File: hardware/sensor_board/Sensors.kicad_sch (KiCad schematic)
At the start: 12 parts

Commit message: all bricked...
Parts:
- gave numbers to parts that had none: 12

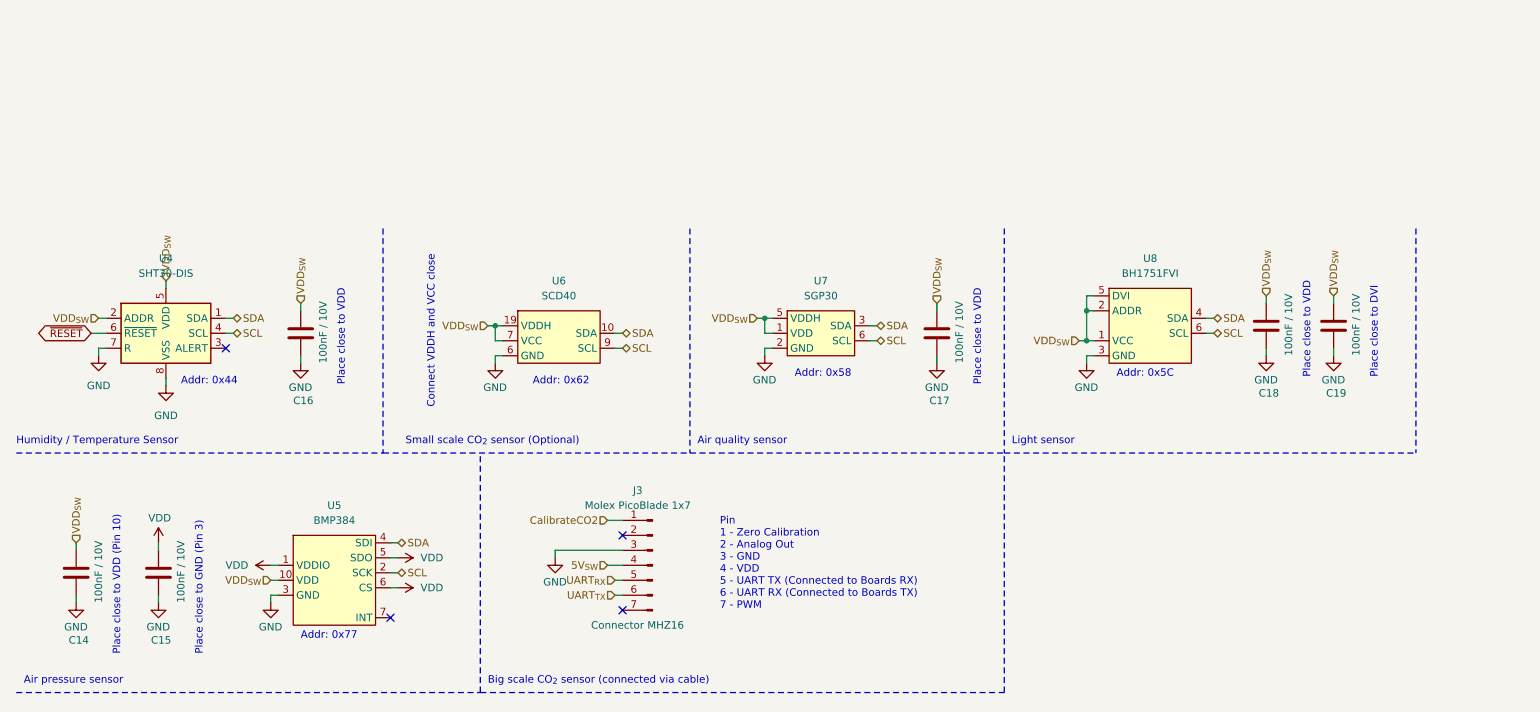
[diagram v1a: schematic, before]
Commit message: solved issues with ERC
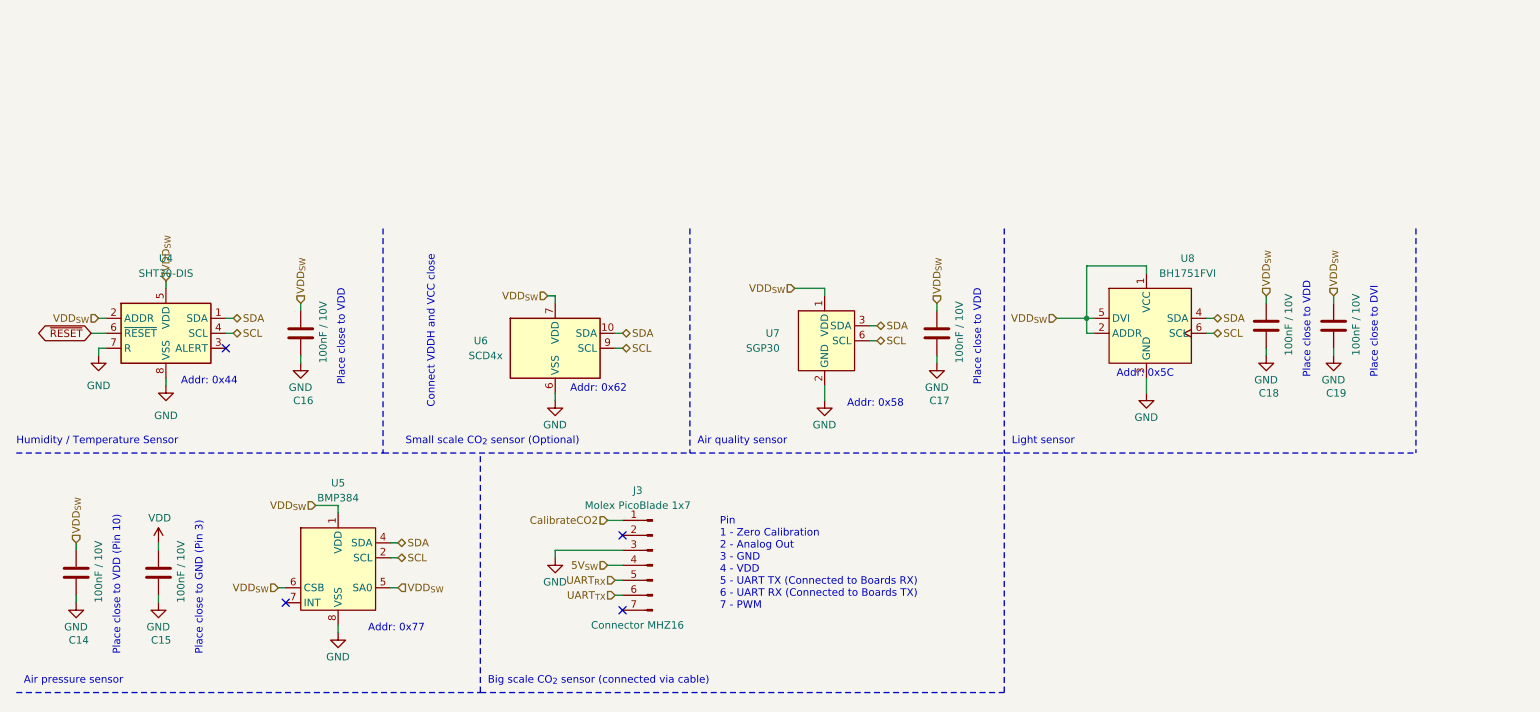
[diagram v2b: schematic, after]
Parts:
- removed U6: SCD40, symbol ownLib:SCD40
- added U6: SCD4x, dp:SCD4x, symbol ownLib:SCD4x
- U5: footprint (none) -> dp:BMP384
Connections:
- net SCL: now also U6.9 (SCL)
- net SDA: now also U6.10 (SDA)
- net VDD: no longer U5.1 (VDDIO), U5.5 (SDO), U5.6 (CS)
- net VDD_{SW}: now also U5.1 (VDD), U5.5 (SA0), U5.6 (CSB), U6.19 (VDD), U6.7 (VDD)
- net EP renamed GND
- net GND: now also U6.20 (VSS), U6.21 (VSS), U6.6 (VSS)

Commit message: did some stuff
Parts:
- C14, C15, C16, C17, C18, C19: footprint (none) -> Capacitor_SMD:C_0603_1608Metric
- J3: footprint (none) -> Connector_Molex:Molex_PicoBlade_53261-0771_1x07-1MP_P1.25mm_Horizontal
- U5: footprint dp:BMP384 -> ownLib:BMP384
- U6: footprint dp:SCD4x -> ownLib:SCD4x
- U7: footprint (none) -> ownLib:DFN-6-P0.8mm_EP1.25x1.7mm
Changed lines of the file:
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@@
       (effects (font (size 1.27 1.27)) (justify left))
     )
-    (property "Footprint" "" (id 2) (at 23.8252 74.93 0)
+    (property "Footprint" "Capacitor_SMD:C_0603_1608Metric" (id 2) (at 23.8252 74.93 0)
       (effects (font (size 1.27 1.27)) hide)
     )
@@
       (effects (font (size 1.27 1.27)) (justify left))
     )
-    (property "Footprint" "" (id 2) (at 37.7952 74.93 0)
+    (property "Footprint" "Capacitor_SMD:C_0603_1608Metric" (id 2) (at 37.7952 74.93 0)
       (effects (font (size 1.27 1.27)) hide)
     )
@@
       (effects (font (size 1.27 1.27)) (justify left))
     )
-    (property "Footprint" "" (id 2) (at 61.9252 34.29 0)
+    (property "Footprint" "Capacitor_SMD:C_0603_1608Metric" (id 2) (at 61.9252 34.29 0)
       (effects (font (size 1.27 1.27)) hide)
     )
@@
       (effects (font (size 1.27 1.27)) (justify left))
     )
-    (property "Footprint" "" (id 2) (at 169.8752 34.29 0)
+    (property "Footprint" "Capacitor_SMD:C_0603_1608Metric" (id 2) (at 169.8752 34.29 0)
       (effects (font (size 1.27 1.27)) hide)
     )
@@
       (effects (font (size 1.27 1.27)) (justify left))
     )
-    (property "Footprint" "" (id 2) (at 225.7552 33.02 0)
+    (property "Footprint" "Capacitor_SMD:C_0603_1608Metric" (id 2) (at 225.7552 33.02 0)
       (effects (font (size 1.27 1.27)) hide)
     )
@@
       (effects (font (size 1.27 1.27)) (justify left))
     )
-    (property "Footprint" "" (id 2) (at 237.1852 33.02 0)
+    (property "Footprint" "Capacitor_SMD:C_0603_1608Metric" (id 2) (at 237.1852 33.02 0)
       (effects (font (size 1.27 1.27)) hide)
     )
@@
     (property "Reference" "J3" (id 0) (at 118.1481 57.15 0))
     (property "Value" "Molex PicoBlade 1x7" (id 1) (at 118.1481 59.69 0))
-    (property "Footprint" "" (id 2) (at 120.65 69.85 0)
+    (property "Footprint" "Connector_Molex:Molex_PicoBlade_53261-0771_1x07-1MP_P1.25mm_Horizontal" (id 2) (at 120.65 69.85 0)
       (effects (font (size 1.27 1.27)) hide)
     )
@@
       (effects (font (size 1.27 1.27)) (justify right))
     )
-    (property "Footprint" "" (id 2) (at 149.86 30.48 0)
+    (property "Footprint" "ownLib:DFN-6-P0.8mm_EP1.25x1.7mm" (id 2) (at 149.86 30.48 0)
       (effects (font (size 1.27 1.27)) hide)
     )
@@
       (effects (font (size 1.27 1.27)) (justify right))
     )
-    (property "Footprint" "dp:SCD4x" (id 2) (at 104.14 24.13 0)
+    (property "Footprint" "ownLib:SCD4x" (id 2) (at 104.14 24.13 0)
       (effects (font (size 1.27 1.27)) hide)
     )
@@
     (property "Reference" "U5" (id 0) (at 67.31 55.88 0))
     (property "Value" "BMP384" (id 1) (at 67.31 58.42 0))
-    (property "Footprint" "dp:BMP384" (id 2) (at 67.31 71.12 0)
+    (property "Footprint" "ownLib:BMP384" (id 2) (at 67.31 71.12 0)
       (effects (font (size 1.27 1.27)) hide)
     )

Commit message: finished schematic and added board
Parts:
- U8: footprint (none) -> ownLib:WSOF6
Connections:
- net VDD is gone; now on net VDD_{SW}: C15.1
- net GND: now also U7.7 (EP); no longer U7.PAD (EP)
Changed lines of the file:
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@@
     (effects (font (size 1.27 1.27)) (justify right))
+  )
+  (hierarchical_label "VDD_{SW}" (shape input) (at 36.83 66.04 90)
+    (effects (font (size 1.27 1.27)) (justify left))
   )
   (hierarchical_label "VDD_{SW}" (shape input) (at 38.1 21.59 90)
@@
   (hierarchical_label "VDD_{SW}" (shape input) (at 236.22 24.13 90)
     (effects (font (size 1.27 1.27)) (justify left))
-  )
-  (symbol (lib_id "power:VDD") (at 36.83 66.04 0) (unit 1)
-    (in_bom yes) (on_board yes)
-    (property "Reference" "#PWR022" (id 0) (at 36.83 69.85 0)
-      (effects (font (size 1.27 1.27)) hide)
-    )
-    (property "Value" "VDD" (id 1) (at 35.0916 61.8281 0)
-      (effects (font (size 1.27 1.27)) (justify left))
-    )
-    (property "Footprint" "" (id 2) (at 36.83 66.04 0)
-      (effects (font (size 1.27 1.27)) hide)
-    )
-    (property "Datasheet" "" (id 3) (at 36.83 66.04 0)
-      (effects (font (size 1.27 1.27)) hide)
-    )
-    (pin "1")
   )
   (symbol (lib_id "power:GND") (at 22.86 76.2 0) (unit 1)
@@
     (pin "5")
     (pin "6")
-    (pin "PAD")
+    (pin "7")
   )
   (symbol (lib_id "ownLib:SCD4x") (at 104.14 33.02 0) (unit 1)
@@
     (property "Reference" "U8" (id 0) (at 211.455 17.78 0))
     (property "Value" "BH1751FVI" (id 1) (at 211.455 20.32 0))
-    (property "Footprint" "" (id 2) (at 204.47 29.21 0)
-      (effects (font (size 1.27 1.27)) hide)
-    )
+    (property "Footprint" "ownLib:WSOF6" (id 2) (at 204.47 29.21 0)
+      (effects (font (size 1.27 1.27)) hide)
+    )

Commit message: review
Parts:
- added C?: 100nF / 6.3V, Capacitor_SMD:C_0603_1608Metric, symbol Device:C
- added C?: 10uF / 6.3V, Capacitor_SMD:C_0603_1608Metric, symbol Device:C
- C14, C15, C16, C17, C18, C19: value 100nF / 10V -> 100nF / 6.3V
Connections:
- net GND: now also C?.2, C?.2
- net VDD_{SW}: now also C?.1, C?.1
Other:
- note added: "ADDR auf GND"
- note added: "Change J3 to new setup! SERCOM to Connector and 2 GPIOs + 5V + 3.3V"
- moved on the sheet: C17, C18, C19, J3, U6, U7, U8

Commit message: updated pcb
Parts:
- C14, C15, C16, C17, C18, C19: footprint Capacitor_SMD:C_0603_1608Metric -> Capacitor_SMD:C_0402_1005Metric
- C28: renamed from C?; footprint Capacitor_SMD:C_0603_1608Metric -> Capacitor_SMD:C_0402_1005Metric
- J3: footprint Connector_Molex:Molex_PicoBlade_53261-0771_1x07-1MP_P1.25mm_Horizontal -> Connector_Molex:Molex_PicoBlade_53261-1071_1x10-1MP_P1.25mm_Horizontal; symbol Connector:Conn_01x07_Male -> Connector:Conn_01x10_Male
- gave numbers to parts that had none: 1
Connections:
- net CalibrateCO2 is gone; now on net GND: J3.1 (Pin_1)
- net UART_{TX} is gone; now on net GND: J3.6 (Pin_6)
- net 5V_{SW}: now also J3.8 (Pin_8); no longer J3.4 (Pin_4)
- net GND: now also U4.2 (ADDR), U7.PAD (EP), U8.2 (ADDR); no longer J3.3 (Pin_3), U7.7 (EP)
- net VDD_{SW}: now also J3.7 (Pin_7); no longer U4.2 (ADDR), U8.2 (ADDR)
- net SERCOM0.0: now reaches J3.2 (Pin_2)
- net UART_{RX} renamed SERCOM0.3
- new net GPIO.0: J3.9 (Pin_9)
- new net GPIO.1: J3.10 (Pin_10)
- new net SERCOM0.1: J3.3 (Pin_3)
- new net SERCOM0.2: J3.4 (Pin_4)
- no-connect marks 4 -> 2
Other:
- note added: "Addr: 0x23"
- note added: "External Sensor over SERCOM"
- note removed: "ADDR auf GND"
- note removed: "Addr: 0x5C"
- note removed: "Big scale CO_{2} sensor (connected via cable)"
- note removed: "Change J3 to new setup! SERCOM to Connector and 2 GPIOs + 5V + 3.3V"
- note removed: "Pin 1 - Zero Calibration 2 - Analog Out 3 - GND 4 - VDD 5 - UART TX (Connected to Boards RX) 6 - UART RX (Connected to Boards TX) 7 - PWM"

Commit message: zeug!
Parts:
- added J?: Conn_01x10_MountingPin, symbol Connector_Generic_MountingPin:Conn_01x10_MountingPin
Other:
- note added: "RESET PIN WEG!!!!"
- note added: "Zweiter 100nF"
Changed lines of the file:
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@@
 (kicad_sch (version 20210621) (generator eeschema)
   (paper "A4")
+  (junction (at 223.52 39.37) (diameter 0) (color 0 0 0 0))
   (junction (at 213.36 27.94) (diameter 0) (color 0 0 0 0))
-  (junction (at 223.52 39.37) (diameter 0) (color 0 0 0 0))
   (no_connect (at 58.42 76.2))
   (no_connect (at 48.26 33.02))
@@
     (effects (font (size 1.27 1.27)) (justify left bottom))
   )
+  (text "RESET PIN WEG!!!!" (at 16.51 17.78 0)
+    (effects (font (size 1.27 1.27)) (justify left bottom))
+  )
   (text "External Sensor over SERCOM" (at 111.76 90.17 0)
     (effects (font (size 1.27 1.27)) (justify left bottom))
@@
   )
   (text "Light sensor" (at 200.66 49.53 0)
+    (effects (font (size 1.27 1.27)) (justify left bottom))
+  )
+  (text "Zweiter 100nF\n" (at 114.3 19.05 0)
     (effects (font (size 1.27 1.27)) (justify left bottom))
   )
@@
     (pin "2")
   )
+  (symbol (lib_id "Connector_Generic_MountingPin:Conn_01x10_MountingPin") (at 163.83 66.04 0) (unit 1)
+    (in_bom yes) (on_board yes) (fields_autoplaced)
+    (property "Reference" "J?" (id 0) (at 166.37 67.8814 0)
+      (effects (font (size 1.27 1.27)) (justify left))
+    )
+    (property "Value" "Conn_01x10_MountingPin" (id 1) (at 166.37 70.4214 0)
+      (effects (font (size 1.27 1.27)) (justify left))
+    )
+    (property "Footprint" "" (id 2) (at 163.83 66.04 0)
+      (effects (font (size 1.27 1.27)) hide)
+    )
+    (property "Datasheet" "~" (id 3) (at 163.83 66.04 0)
+      (effects (font (size 1.27 1.27)) hide)
+    )
+    (pin "1")
+    (pin "10")
+    (pin "2")
+    (pin "3")
+    (pin "4")
+    (pin "5")
+    (pin "6")
+    (pin "7")
+    (pin "8")
+    (pin "9")
+    (pin "MP")
+  )
   (symbol (lib_id "power:GND") (at 25.4 27.94 270) (unit 1)

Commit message: updated pcb
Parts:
- removed J3: Molex PicoBlade 1x7, Connector_Molex:Molex_PicoBlade_53261-1071_1x10-1MP_P1.25mm_Horizontal, symbol Connector:Conn_01x10_Male
- added C22, C23: 100nF / 6.3V, Capacitor_SMD:C_0402_1005Metric, symbol Device:C
- J3: renamed from J?; footprint (none) -> Connector_Molex:Molex_PicoBlade_53261-1071_1x10-1MP_P1.25mm_Horizontal
- renumbered C14 to C17, C15 to C18, C16 to C19, C28 to C20, C29 to C21, C17 to C24, C18 to C25, C19 to C26, U4 to U5, U5 to U6, U6 to U7, U7 to U8, U8 to U9
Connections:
- net ~{RESET} is gone; now on net VDD_{SW}: U5.6 (~{RESET})
- net 5V_{SW}: now also J3.5 (Pin_5)
- net GND: now also J3.1 (Pin_1), J3.10 (Pin_10), J3.MP (MountPin), U8.7 (EP), C22.2, C23.2; no longer U8.PAD (EP)
- net GPIO.0: now also J3.2 (Pin_2)
- net GPIO.1: now also J3.3 (Pin_3)
- net SERCOM0.0: now also J3.6 (Pin_6)
- net SERCOM0.1: now also J3.7 (Pin_7)
- net SERCOM0.2: now also J3.8 (Pin_8)
- net SERCOM0.3: now also J3.9 (Pin_9)
- net VDD_{SW}: now also J3.4 (Pin_4), C22.1, C23.1
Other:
- note removed: "RESET PIN WEG!!!!"
- note removed: "Zweiter 100nF"
- moved on the sheet: J3
